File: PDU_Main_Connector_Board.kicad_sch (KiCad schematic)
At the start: 2 parts

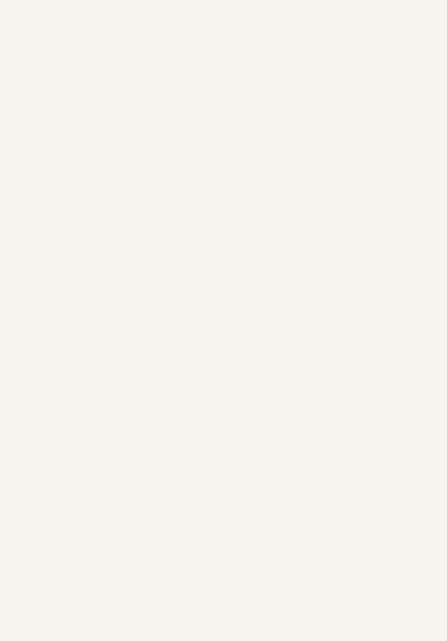
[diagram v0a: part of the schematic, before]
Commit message: VER1.0: исправил Э3
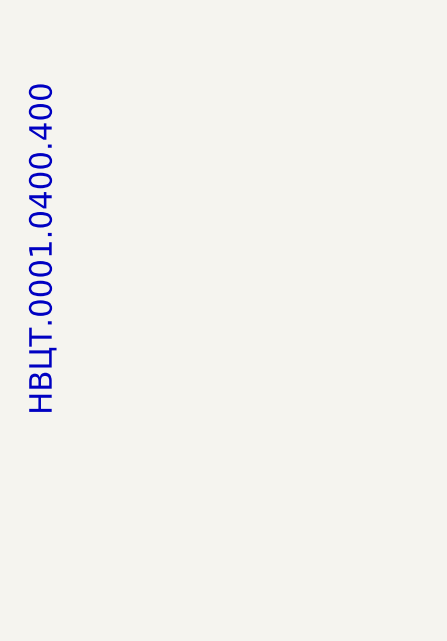
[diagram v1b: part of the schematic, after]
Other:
- note added: "НВЦТ.0001.0400.400"
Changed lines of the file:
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@@
+		)
+	)
+	(text "НВЦТ.0001.0400.400"
+		(exclude_from_sim no)
+		(at 16.51 35.56 90)
+		(effects
+			(font
+				(size 2.5 2.5)
+			)
 		)
 	)

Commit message: VER1.0: исправил Э3
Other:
- note added: "1. Перечень элементов см. НВЦТ.0001.0400.400 ПЭ3."
- note added: "ООО "Электротранспортные"
- note added: "технологии""
- company: ООО "Электротранспортные технологии" -> (none)
- moved on the sheet: J1, J2
